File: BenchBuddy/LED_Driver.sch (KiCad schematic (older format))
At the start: 0 parts

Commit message: Week3 Part 2
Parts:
- added C? (x2): C, ~, symbol C
- added D?: DIODESCH, ~, symbol DIODESCH
- added L?: INDUCTOR, ~, symbol INDUCTOR
- added R?: R, ~, symbol R
- added U?: AP5726, ~, symbol AP5726
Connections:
- new net: D?.1 (A), L?.2, U?.1 (SW)
- new net +5V: C?.1, L?.1, U?.6 (VIN6)
- new net GND: C?.2, C?.2, R?.2, U?.2 (GND)
- new net LED_EN_PWM: U?.4 (EN)
- new net LED_String+: C?.1, D?.2 (K), U?.5 (OVP)
- new net LED_String-: R?.1, U?.3 (FB)
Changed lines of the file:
@@
 EESchema Schematic File Version 2
+LIBS:BenchBuddy
 LIBS:power
 LIBS:device
@@
 Sheet 6 9
 Title ""
-Date "5 mar 2014"
+Date "7 mar 2014"
 Rev ""
 Comp ""
@@
 $EndDescr
 Text HLabel 1650 2050 0    60   Input ~ 0
-EN
-Text HLabel 1750 2300 0    60   Input ~ 0
-FREQ
-Text HLabel 10300 2100 0    60   Output ~ 0
-String+
-Text HLabel 10300 2450 0    60   Input ~ 0
-String-
+LED_EN_PWM
+Text HLabel 9700 900  2    60   Output ~ 0
+LED_String+
+Text HLabel 9700 2250 2    60   Output ~ 0
+LED_String-
+$Comp
+L AP5726 U?
+U 1 1 5317C0FB
+P 2850 2050
+F 0 "U?" H 3100 1600 60  0000 C CNN
+F 1 "AP5726" H 2850 2150 60  0000 C CNN
+F 2 "~" H 2850 2050 60  0000 C CNN
+F 3 "~" H 2850 2050 60  0000 C CNN
+	1    2850 2050
+	1    0    0    -1
+$EndComp
+$Comp
+L +5V #PWR?
+U 1 1 5317C39B
+P 1650 850
+F 0 "#PWR?" H 1650 940 20  0001 C CNN
+F 1 "+5V" H 1650 940 30  0000 C CNN
+F 2 "~" H 1650 850 60  0000 C CNN
+F 3 "~" H 1650 850 60  0000 C CNN
+	1    1650 850
+	1    0    0    -1
+$EndComp
+$Comp
+L GND #PWR?
+U 1 1 5317C3AA
+P 1650 1650
+F 0 "#PWR?" H 1650 1650 30  0001 C CNN
+F 1 "GND" H 1650 1580 30  0001 C CNN
+F 2 "~" H 1650 1650 60  0000 C CNN
+F 3 "~" H 1650 1650 60  0000 C CNN
+	1    1650 1650
+	1    0    0    -1
+$EndComp
+$Comp
+L GND #PWR?
+U 1 1 5317C3B7
+P 2850 2950
+F 0 "#PWR?" H 2850 2950 30  0001 C CNN
+F 1 "GND" H 2850 2880 30  0001 C CNN
+F 2 "~" H 2850 2950 60  0000 C CNN
+F 3 "~" H 2850 2950 60  0000 C CNN
+	1    2850 2950
+	1    0    0    -1
+$EndComp
+$Comp
+L C C?
+U 1 1 5317C3C1
+P 1650 1200
+F 0 "C?" H 1650 1300 40  0000 L CNN
+F 1 "C" H 1656 1115 40  0000 L CNN
+F 2 "~" H 1688 1050 30  0000 C CNN
+F 3 "~" H 1650 1200 60  0000 C CNN
+	1    1650 1200
+	1    0    0    -1
+$EndComp
+$Comp
+L INDUCTOR L?
+U 1 1 5317C3D0
+P 3100 900
+F 0 "L?" V 3050 900 40  0000 C CNN
+F 1 "INDUCTOR" V 3200 900 40  0000 C CNN
+F 2 "~" H 3100 900 60  0000 C CNN
+F 3 "~" H 3100 900 60  0000 C CNN
+	1    3100 900
+	0    -1   -1   0
+$EndComp
+$Comp
+L R R?
+U 1 1 5317C3E4
+P 3850 2600
+F 0 "R?" V 3930 2600 40  0000 C CNN
+F 1 "R" V 3857 2601 40  0000 C CNN
+F 2 "~" V 3780 2600 30  0000 C CNN
+F 3 "~" H 3850 2600 30  0000 C CNN
+	1    3850 2600
+	1    0    0    -1
+$EndComp
+Wire Wire Line
+	1650 2050 2200 2050
+Wire Wire Line
+	2850 2950 2850 2700
+Wire Wire Line
+	1650 1000 1650 850
+Wire Wire Line
+	1650 1400 1650 1650
+Wire Wire Line
+	1650 900  2800 900
+Wire Wire Line
+	2700 900  2700 1350
+Connection ~ 1650 900
+Connection ~ 2700 900
+Wire Wire Line
+	3000 1350 3000 1150
+Wire Wire Line
+	3000 1150 3650 1150
+Wire Wire Line
+	3650 1150 3650 900
+Wire Wire Line
+	3400 900  3800 900
+$Comp
+L DIODESCH D?
+U 1 1 5317C44B
+P 4000 900
+F 0 "D?" H 4000 1000 40  0000 C CNN
+F 1 "DIODESCH" H 4000 800 40  0000 C CNN
+F 2 "~" H 4000 900 60  0000 C CNN
+F 3 "~" H 4000 900 60  0000 C CNN
+	1    4000 900
+	1    0    0    -1
+$EndComp
+Connection ~ 3650 900
+Wire Wire Line
+	4200 900  9700 900
+Wire Wire Line
+	4350 900  4350 2050
+Wire Wire Line
+	4350 2050 3500 2050
+Wire Wire Line
+	3500 2250 9700 2250
+Wire Wire Line
+	3850 2250 3850 2350
+Wire Wire Line
+	3850 2850 3850 2900
+Wire Wire Line
+	3850 2900 2850 2900
+Connection ~ 2850 2900
+Connection ~ 3850 2250
+Connection ~ 4350 900
+$Comp
+L C C?
+U 1 1 5317C4EC
+P 8950 1400
+F 0 "C?" H 8950 1500 40  0000 L CNN
+F 1 "C" H 8956 1315 40  0000 L CNN
+F 2 "~" H 8988 1250 30  0000 C CNN
+F 3 "~" H 8950 1400 60  0000 C CNN
+	1    8950 1400
+	1    0    0    -1
+$EndComp
+Wire Wire Line
+	8950 900  8950 1200
+Connection ~ 8950 900
+Wire Wire Line
+	8950 1600 8950 1800
+$Comp
+L GND #PWR?
+U 1 1 5317C525
+P 8950 1800
+F 0 "#PWR?" H 8950 1800 30  0001 C CNN
+F 1 "GND" H 8950 1730 30  0001 C CNN
+F 2 "~" H 8950 1800 60  0000 C CNN
+F 3 "~" H 8950 1800 60  0000 C CNN
+	1    8950 1800
+	1    0    0    -1
+$EndComp
 $EndSCHEMATC

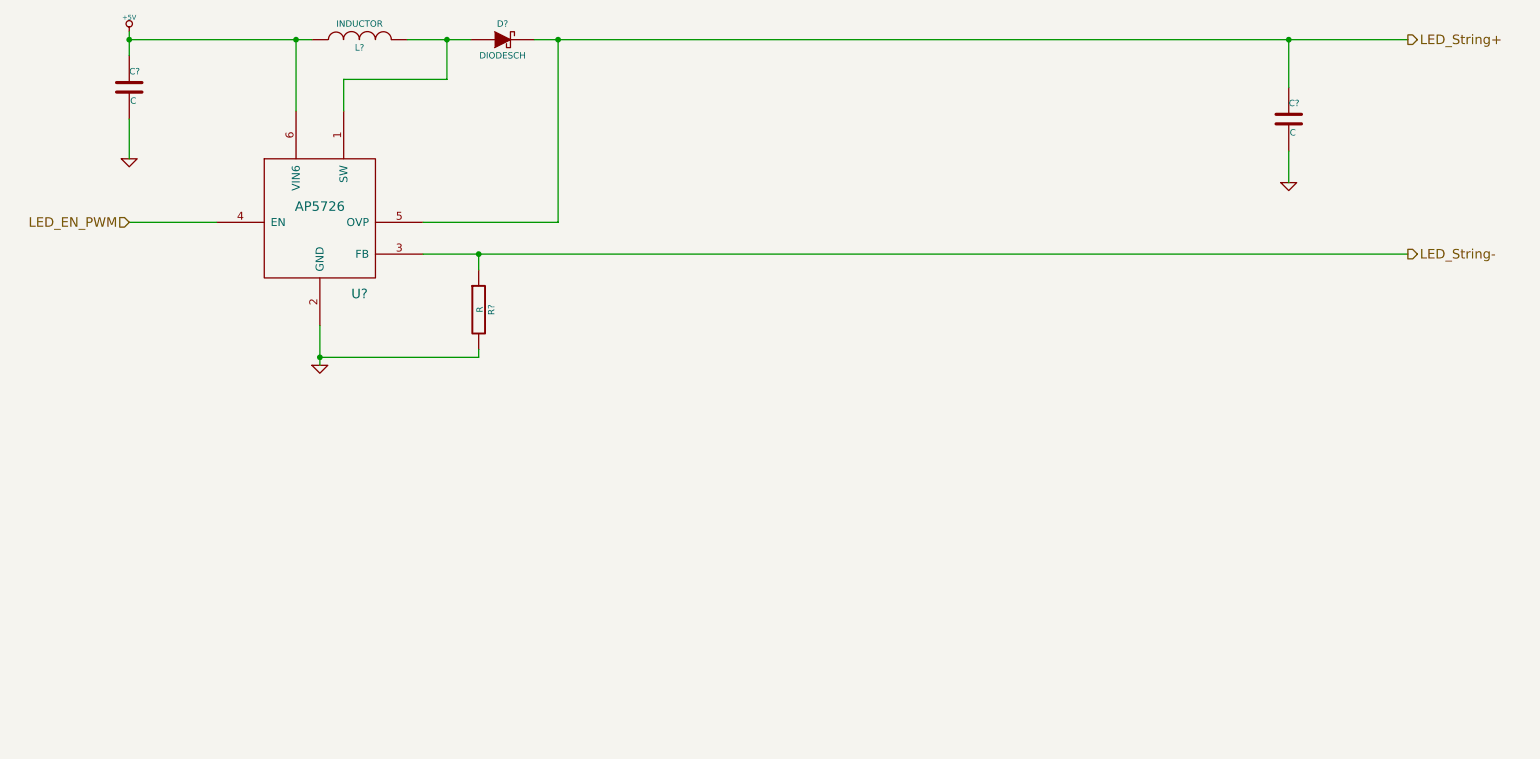
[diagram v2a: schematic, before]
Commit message: Colocação dos Componentes Relé
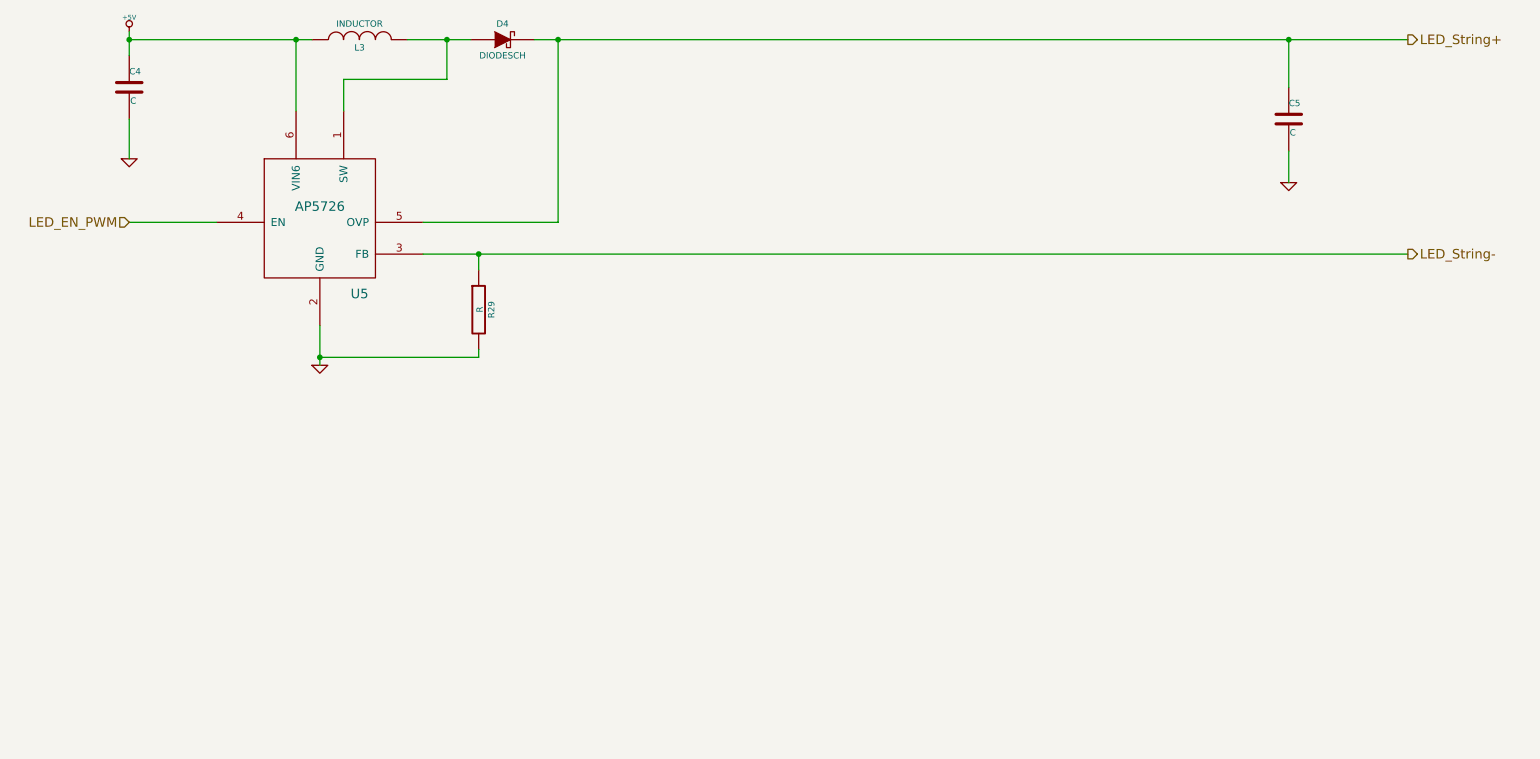
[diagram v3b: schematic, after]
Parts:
- gave numbers to parts that had none: 6
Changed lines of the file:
@@
 Sheet 6 9
 Title ""
-Date "7 mar 2014"
+Date "9 mar 2014"
 Rev ""
 Comp ""
@@
 LED_String-
 $Comp
-L AP5726 U?
+L AP5726 U5
 U 1 1 5317C0FB
 P 2850 2050
-F 0 "U?" H 3100 1600 60  0000 C CNN
+F 0 "U5" H 3100 1600 60  0000 C CNN
 F 1 "AP5726" H 2850 2150 60  0000 C CNN
 F 2 "~" H 2850 2050 60  0000 C CNN
@@
 $EndComp
 $Comp
-L +5V #PWR?
+L +5V #PWR26
 U 1 1 5317C39B
 P 1650 850
-F 0 "#PWR?" H 1650 940 20  0001 C CNN
+F 0 "#PWR26" H 1650 940 20  0001 C CNN
 F 1 "+5V" H 1650 940 30  0000 C CNN
 F 2 "~" H 1650 850 60  0000 C CNN
@@
 $EndComp
 $Comp
-L GND #PWR?
+L GND #PWR27
 U 1 1 5317C3AA
 P 1650 1650
-F 0 "#PWR?" H 1650 1650 30  0001 C CNN
+F 0 "#PWR27" H 1650 1650 30  0001 C CNN
 F 1 "GND" H 1650 1580 30  0001 C CNN
 F 2 "~" H 1650 1650 60  0000 C CNN
@@
 $EndComp
 $Comp
-L GND #PWR?
+L GND #PWR28
 U 1 1 5317C3B7
 P 2850 2950
-F 0 "#PWR?" H 2850 2950 30  0001 C CNN
+F 0 "#PWR28" H 2850 2950 30  0001 C CNN
 F 1 "GND" H 2850 2880 30  0001 C CNN
 F 2 "~" H 2850 2950 60  0000 C CNN
@@
 $EndComp
 $Comp
-L C C?
+L C C4
 U 1 1 5317C3C1
 P 1650 1200
-F 0 "C?" H 1650 1300 40  0000 L CNN
+F 0 "C4" H 1650 1300 40  0000 L CNN
 F 1 "C" H 1656 1115 40  0000 L CNN
 F 2 "~" H 1688 1050 30  0000 C CNN
@@
 $EndComp
 $Comp
-L INDUCTOR L?
+L INDUCTOR L3
 U 1 1 5317C3D0
 P 3100 900
-F 0 "L?" V 3050 900 40  0000 C CNN
+F 0 "L3" V 3050 900 40  0000 C CNN
 F 1 "INDUCTOR" V 3200 900 40  0000 C CNN
 F 2 "~" H 3100 900 60  0000 C CNN
@@
 $EndComp
 $Comp
-L R R?
+L R R29
 U 1 1 5317C3E4
 P 3850 2600
-F 0 "R?" V 3930 2600 40  0000 C CNN
+F 0 "R29" V 3930 2600 40  0000 C CNN
 F 1 "R" V 3857 2601 40  0000 C CNN
 F 2 "~" V 3780 2600 30  0000 C CNN
@@
 	3400 900  3800 900
 $Comp
-L DIODESCH D?
+L DIODESCH D4
 U 1 1 5317C44B
 P 4000 900
-F 0 "D?" H 4000 1000 40  0000 C CNN
+F 0 "D4" H 4000 1000 40  0000 C CNN
 F 1 "DIODESCH" H 4000 800 40  0000 C CNN
 F 2 "~" H 4000 900 60  0000 C CNN
@@
 Connection ~ 4350 900
 $Comp
-L C C?
+L C C5
 U 1 1 5317C4EC
 P 8950 1400
-F 0 "C?" H 8950 1500 40  0000 L CNN
+F 0 "C5" H 8950 1500 40  0000 L CNN
 F 1 "C" H 8956 1315 40  0000 L CNN
 F 2 "~" H 8988 1250 30  0000 C CNN
@@
 	8950 1600 8950 1800
 $Comp
-L GND #PWR?
+L GND #PWR29
 U 1 1 5317C525
 P 8950 1800
-F 0 "#PWR?" H 8950 1800 30  0001 C CNN
+F 0 "#PWR29" H 8950 1800 30  0001 C CNN
 F 1 "GND" H 8950 1730 30  0001 C CNN
 F 2 "~" H 8950 1800 60  0000 C CNN

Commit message: Pre layout
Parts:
- C4, C5: value C -> 1 uF
- D4: value DIODESCH -> B4540WS-7
- L3: value INDUCTOR -> 22uH; MFG Part Number (none) -> NR4012T220M
- R29: value R -> 15R
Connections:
- net +5V renamed +5P
- net GND renamed GND_LED
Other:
- moved on the sheet: C4, C5, D4, L3, R29, U5
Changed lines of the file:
@@
 $Descr A4 11693 8268
 encoding utf-8
-Sheet 6 9
+Sheet 3 9
 Title ""
-Date "9 mar 2014"
+Date "30 mar 2014"
 Rev ""
 Comp ""
@@
 Comment4 ""
 $EndDescr
-Text HLabel 1650 2050 0    60   Input ~ 0
+Text HLabel 3350 4350 0    60   Input ~ 0
 LED_EN_PWM
-Text HLabel 9700 900  2    60   Output ~ 0
+Text HLabel 9050 3200 2    60   Output ~ 0
 LED_String+
-Text HLabel 9700 2250 2    60   Output ~ 0
+Text HLabel 9050 4550 2    60   Output ~ 0
 LED_String-
 $Comp
 L AP5726 U5
 U 1 1 5317C0FB
-P 2850 2050
-F 0 "U5" H 3100 1600 60  0000 C CNN
-F 1 "AP5726" H 2850 2150 60  0000 C CNN
-F 2 "~" H 2850 2050 60  0000 C CNN
-F 3 "~" H 2850 2050 60  0000 C CNN
-	1    2850 2050
-	1    0    0    -1
-$EndComp
-$Comp
-L +5V #PWR26
-U 1 1 5317C39B
-P 1650 850
-F 0 "#PWR26" H 1650 940 20  0001 C CNN
-F 1 "+5V" H 1650 940 30  0000 C CNN
-F 2 "~" H 1650 850 60  0000 C CNN
-F 3 "~" H 1650 850 60  0000 C CNN
-	1    1650 850
-	1    0    0    -1
-$EndComp
-$Comp
-L GND #PWR27
-U 1 1 5317C3AA
-P 1650 1650
-F 0 "#PWR27" H 1650 1650 30  0001 C CNN
-F 1 "GND" H 1650 1580 30  0001 C CNN
-F 2 "~" H 1650 1650 60  0000 C CNN
-F 3 "~" H 1650 1650 60  0000 C CNN
-	1    1650 1650
-	1    0    0    -1
-$EndComp
-$Comp
-L GND #PWR28
-U 1 1 5317C3B7
-P 2850 2950
-F 0 "#PWR28" H 2850 2950 30  0001 C CNN
-F 1 "GND" H 2850 2880 30  0001 C CNN
-F 2 "~" H 2850 2950 60  0000 C CNN
-F 3 "~" H 2850 2950 60  0000 C CNN
-	1    2850 2950
+P 4550 4350
+F 0 "U5" H 4800 3900 60  0000 C CNN
+F 1 "AP5726" H 4550 4450 60  0000 C CNN
+F 2 "~" H 4550 4350 60  0000 C CNN
+F 3 "~" H 4550 4350 60  0000 C CNN
+	1    4550 4350
 	1    0    0    -1
 $EndComp
@@
 L C C4
 U 1 1 5317C3C1
-P 1650 1200
-F 0 "C4" H 1650 1300 40  0000 L CNN
-F 1 "C" H 1656 1115 40  0000 L CNN
-F 2 "~" H 1688 1050 30  0000 C CNN
-F 3 "~" H 1650 1200 60  0000 C CNN
-	1    1650 1200
+P 3350 3500
+F 0 "C4" H 3350 3600 40  0000 L CNN
+F 1 "1 uF" H 3356 3415 40  0000 L CNN
+F 2 "~" H 3388 3350 30  0000 C CNN
+F 3 "~" H 3350 3500 60  0000 C CNN
+	1    3350 3500
 	1    0    0    -1
 $EndComp
@@
 L INDUCTOR L3
 U 1 1 5317C3D0
-P 3100 900
-F 0 "L3" V 3050 900 40  0000 C CNN
-F 1 "INDUCTOR" V 3200 900 40  0000 C CNN
-F 2 "~" H 3100 900 60  0000 C CNN
-F 3 "~" H 3100 900 60  0000 C CNN
-	1    3100 900
+P 4800 3200
+F 0 "L3" V 4750 3200 40  0000 C CNN
+F 1 "22uH" V 4900 3200 40  0000 C CNN
+F 2 "~" H 4800 3200 60  0000 C CNN
+F 3 "~" H 4800 3200 60  0000 C CNN
+F 4 "NR4012T220M" H 4800 3200 60  0001 C CNN "MFG Part Number"
+	1    4800 3200
 	0    -1   -1   0
 $EndComp
@@
 L R R29
 U 1 1 5317C3E4
-P 3850 2600
-F 0 "R29" V 3930 2600 40  0000 C CNN
-F 1 "R" V 3857 2601 40  0000 C CNN
-F 2 "~" V 3780 2600 30  0000 C CNN
-F 3 "~" H 3850 2600 30  0000 C CNN
-	1    3850 2600
+P 5550 4900
+F 0 "R29" V 5630 4900 40  0000 C CNN
+F 1 "15R" V 5557 4901 40  0000 C CNN
+F 2 "~" V 5480 4900 30  0000 C CNN
+F 3 "~" H 5550 4900 30  0000 C CNN
+	1    5550 4900
 	1    0    0    -1
 $EndComp
 Wire Wire Line
-	1650 2050 2200 2050
+	3350 4350 3900 4350
 Wire Wire Line
-	2850 2950 2850 2700
+	4550 5000 4550 5250
 Wire Wire Line
-	1650 1000 1650 850
+	3350 3150 3350 3300
 Wire Wire Line
-	1650 1400 1650 1650
+	3350 3700 3350 3950
 Wire Wire Line
-	1650 900  2800 900
+	3350 3200 4500 3200
 Wire Wire Line
-	2700 900  2700 1350
-Connection ~ 1650 900
-Connection ~ 2700 900
+	4400 3200 4400 3650
+Connection ~ 3350 3200
+Connection ~ 4400 3200
 Wire Wire Line
-	3000 1350 3000 1150
+	4700 3650 4700 3450
 Wire Wire Line
-	3000 1150 3650 1150
+	4700 3450 5350 3450
 Wire Wire Line
-	3650 1150 3650 900
+	5350 3450 5350 3200
 Wire Wire Line
-	3400 900  3800 900
+	5100 3200 5500 3200
 $Comp
 L DIODESCH D4
 U 1 1 5317C44B
-P 4000 900
-F 0 "D4" H 4000 1000 40  0000 C CNN
-F 1 "DIODESCH" H 4000 800 40  0000 C CNN
-F 2 "~" H 4000 900 60  0000 C CNN
-F 3 "~" H 4000 900 60  0000 C CNN
-	1    4000 900
+P 5700 3200
+F 0 "D4" H 5700 3300 40  0000 C CNN
+F 1 "B4540WS-7" H 5700 3100 40  0000 C CNN
+F 2 "~" H 5700 3200 60  0000 C CNN
+F 3 "~" H 5700 3200 60  0000 C CNN
+	1    5700 3200
 	1    0    0    -1
 $EndComp
-Connection ~ 3650 900
+Connection ~ 5350 3200
 Wire Wire Line
-	4200 900  9700 900
+	5900 3200 9050 3200
 Wire Wire Line
-	4350 900  4350 2050
+	6050 3200 6050 4350
 Wire Wire Line
-	4350 2050 3500 2050
+	6050 4350 5200 4350
 Wire Wire Line
-	3500 2250 9700 2250
+	5200 4550 9050 4550
 Wire Wire Line
-	3850 2250 3850 2350
+	5550 4550 5550 4650
 Wire Wire Line
-	3850 2850 3850 2900
+	5550 5150 5550 5200
 Wire Wire Line
-	3850 2900 2850 2900
-Connection ~ 2850 2900
-Connection ~ 3850 2250
-Connection ~ 4350 900
+	5550 5200 4550 5200
+Connection ~ 4550 5200
+Connection ~ 5550 4550
+Connection ~ 6050 3200
 $Comp
 L C C5
 U 1 1 5317C4EC
-P 8950 1400
-F 0 "C5" H 8950 1500 40  0000 L CNN
-F 1 "C" H 8956 1315 40  0000 L CNN
-F 2 "~" H 8988 1250 30  0000 C CNN
-F 3 "~" H 8950 1400 60  0000 C CNN
-	1    8950 1400
+P 8300 3700
+F 0 "C5" H 8300 3800 40  0000 L CNN
+F 1 "1 uF" H 8306 3615 40  0000 L CNN
+F 2 "~" H 8338 3550 30  0000 C CNN
+F 3 "~" H 8300 3700 60  0000 C CNN
+	1    8300 3700
 	1    0    0    -1
 $EndComp
 Wire Wire Line
-	8950 900  8950 1200
-Connection ~ 8950 900
+	8300 3200 8300 3500
+Connection ~ 8300 3200
 Wire Wire Line
-	8950 1600 8950 1800
+	8300 3900 8300 4100
 $Comp
-L GND #PWR29
-U 1 1 5317C525
-P 8950 1800
-F 0 "#PWR29" H 8950 1800 30  0001 C CNN
-F 1 "GND" H 8950 1730 30  0001 C CNN
-F 2 "~" H 8950 1800 60  0000 C CNN
-F 3 "~" H 8950 1800 60  0000 C CNN
-	1    8950 1800
+L +5P #PWR22
+U 1 1 532F5F2A
+P 3350 3150
+F 0 "#PWR22" H 3350 3280 20  0001 C CNN
+F 1 "+5P" H 3350 3250 30  0000 C CNN
+F 2 "~" H 3350 3150 60  0000 C CNN
+F 3 "~" H 3350 3150 60  0000 C CNN
+	1    3350 3150
 	1    0    0    -1
 $EndComp
+$Comp
+L GND_LED #PWR020
+U 1 1 53370709
+P 4550 5250
+F 0 "#PWR020" H 4550 5250 30  0001 C CNN
+F 1 "GND_LED" H 4550 5180 30  0000 C CNN
+F 2 "~" H 4550 5250 60  0000 C CNN
+F 3 "~" H 4550 5250 60  0000 C CNN
+	1    4550 5250
+	1    0    0    -1
+$EndComp
+$Comp
+L GND_LED #PWR021
+U 1 1 5337072A
+P 3350 3950
+F 0 "#PWR021" H 3350 3950 30  0001 C CNN
+F 1 "GND_LED" H 3350 3880 30  0000 C CNN
+F 2 "~" H 3350 3950 60  0000 C CNN
+F 3 "~" H 3350 3950 60  0000 C CNN
+	1    3350 3950
+	1    0    0    -1
+$EndComp
+$Comp
+L GND_LED #PWR022
+U 1 1 53370730
+P 8300 4100
+F 0 "#PWR022" H 8300 4100 30  0001 C CNN
+F 1 "GND_LED" H 8300 4030 30  0000 C CNN
+F 2 "~" H 8300 4100 60  0000 C CNN
+F 3 "~" H 8300 4100 60  0000 C CNN
+	1    8300 4100
+	1    0    0    -1
+$EndComp
